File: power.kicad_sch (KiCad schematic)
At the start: 49 parts, among them J201 Barrel_Jack_MountingPin, J202 -, J203 -, Q201 AOD4185, U101 74HC04, U102 74HC08, U103 74HC32, U201 MP9942GJ

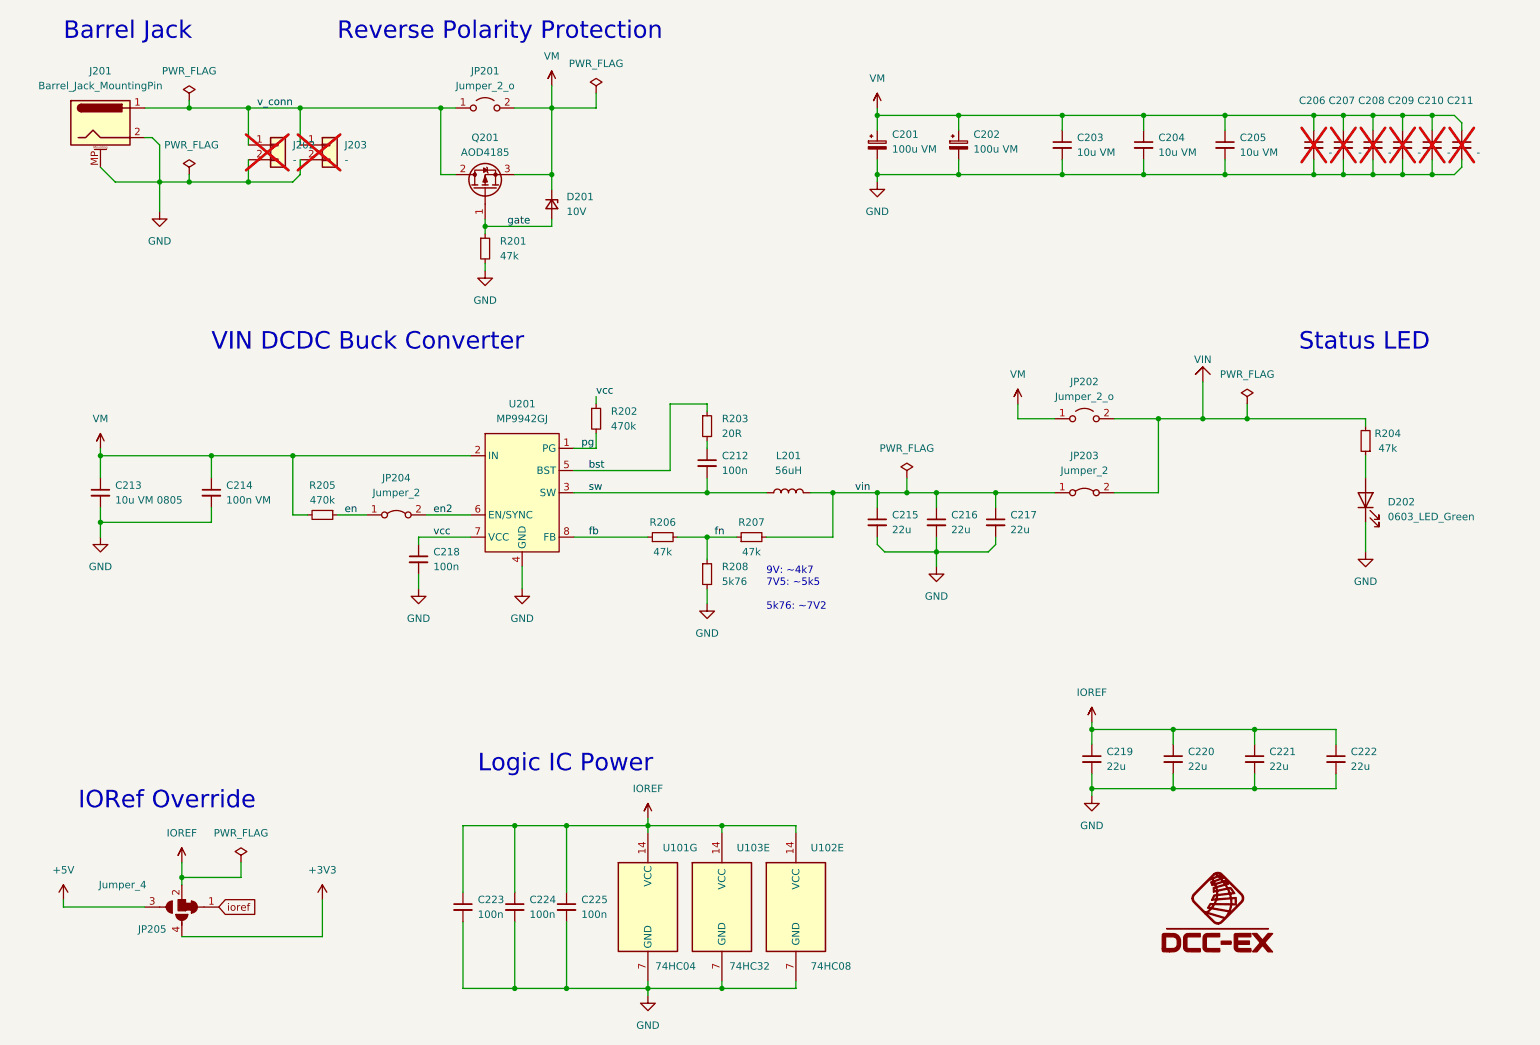
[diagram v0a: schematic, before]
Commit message: Convert to native KiCad & rework BOM to JLCPCB Basic Parts.
1) Use a KiCad template for an Arduino motor shield as the base.

2) DC-DC Buck converter shows no longer available, select new
   component from JLCPCB's basic list and re-work circuit as necessary.

3) Reworked BOM to use as many JLCPCB basic components as possible.

4) Reworked BOM so all components are in-stock at JLCPCB.

5) Switched to TSSOP for the 74HC logic to save space.e

6) Switched to all KiCad native symbols, which required:
   - Reworking some of the solder jumper logic.
   - Renaming VM to Vdrive.
   - Renaming IOREF to VBUS.
   - Renaming VIN to VCOM.
   - Creating a new symbol library for this project.
   - Creating a new footprint library for this project.
   - Moving a LOT of symbols from _my symbols to KiCad native symbols.

7) Removed unnecessary decoupling capacitors from 74HC logic, a single
   100nF is sufficient.

8) Removed unnecessary decoupling capacitors from Vdrive, not sure why
   they were there.

9) Did a new layout of the board:
   - Started with the DRV8874 chips, layout per data sheet, include
     large multi-layer ground plane to dissipate heat.
   - Moved on to DC-DC buck converter, layout per data sheet, include
     large ground plane to dissipate heat.
   - Put the configuration jumpers in ROUGHLY the same place.
   - Put the I2C OLED and STEMMA connectors in the same place, moved
     the 0.1" pin header connector slightly.

10) Routed everything.

11) Made sure it 100% passed ERC.

12) Made sure it 100% passed DRC.
    - A few exclusions for mechanical holes and silk off the board from the
      template.

13) Uploaded to JLCPCB to price.  Adjusted BOM again due to inventory shortages.
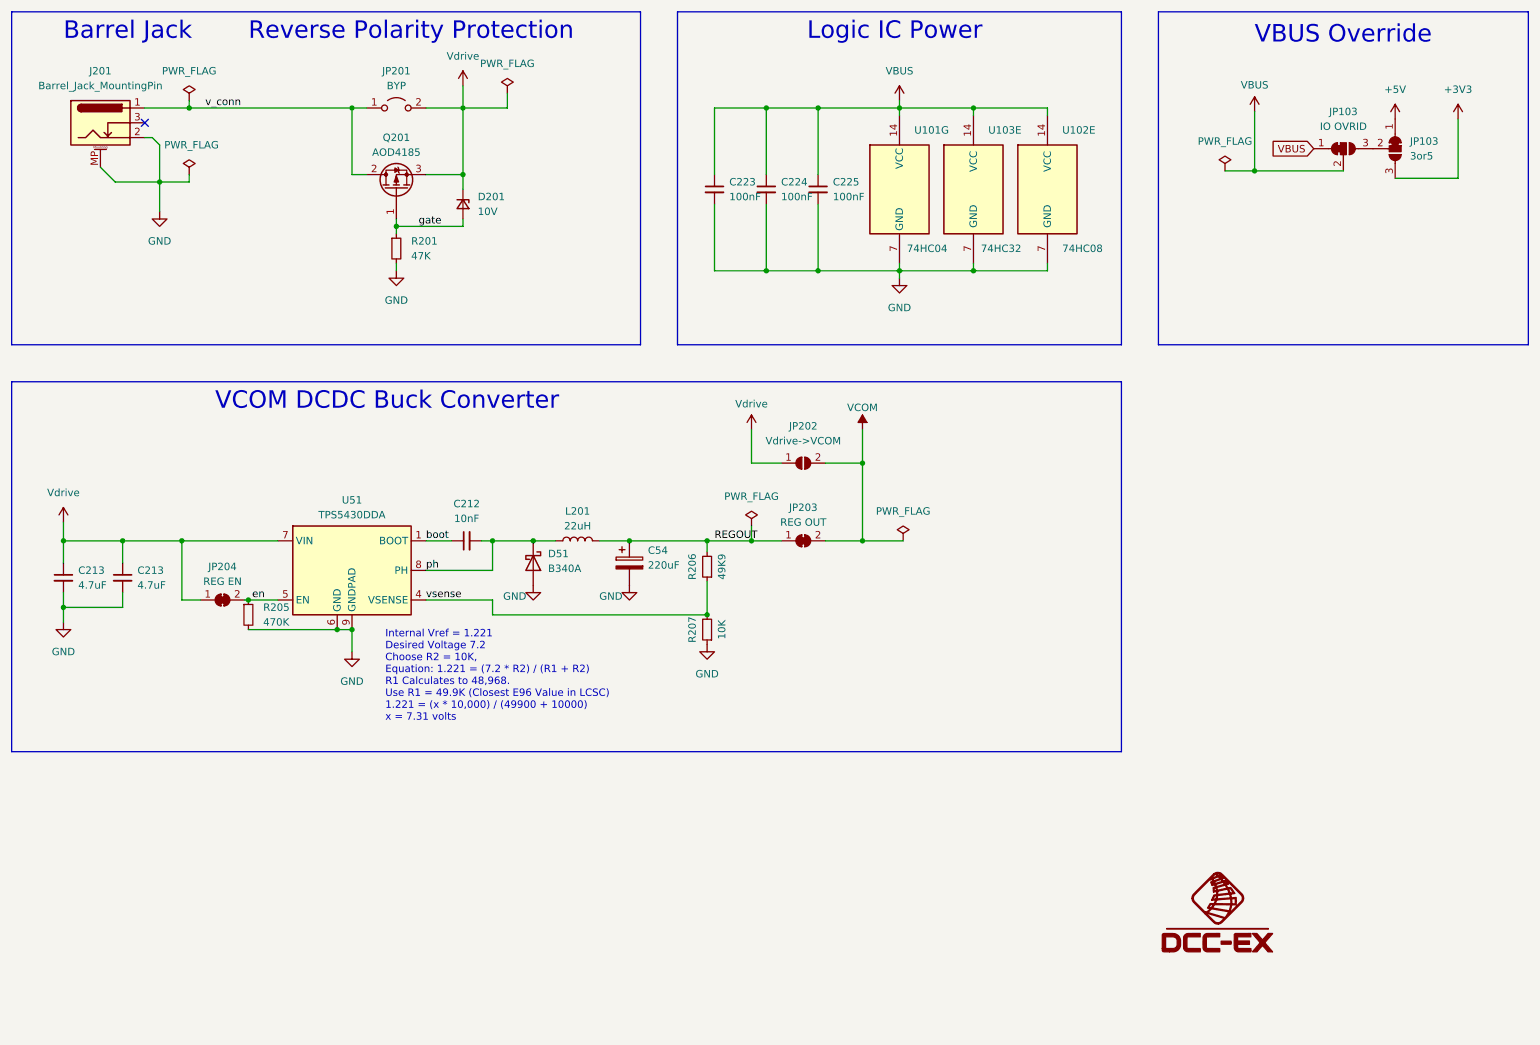
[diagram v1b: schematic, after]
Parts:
- removed C201, C202: 100u VM, Capacitor_SMD:CP_Elec_6.3x7.7, symbol Device:C_Polarized_Small
- removed C203, C204, C205: 10u VM, Capacitor_SMD:C_1206_3216Metric, symbol Device:C_Small
- removed C206, C207, C208, C209, C210, C211: -, Capacitor_SMD:C_1210_3225Metric_Pad1.33x2.70mm_HandSolder, symbol Device:C_Small
- removed C214: 100n VM, _my:C_1005_(0402), symbol Device:C_Small
- removed C215, C216, C217, C219, C220, C221, C222: 22u, Capacitor_SMD:C_0805_2012Metric, symbol Device:C_Small
- removed C218: 100n, _my:C_1005_(0402), symbol Device:C_Small
- removed D202: 0603_LED_Green, LED_SMD:LED_0603_1608Metric, symbol Device:LED
- removed J202: -, _my:PinHeader_01x02_P5mm_Vertical_min, symbol Connector_Generic:Conn_01x02
- removed J203: -, _my:PinHeader_1x04_P2.54mm_Vertical_min_1, symbol Connector_Generic:Conn_01x02
- removed JP205: Jumper_4, _my:SolderJumper-4, symbol _my:SolderJumper_4
- removed R202: 470k, _my:R_1005_(0402), symbol Device:R_Small
- removed R203: 20R, _my:R_1005_(0402), symbol Device:R_Small
- removed R204: 47k, _my:R_1005_(0402), symbol Device:R_Small
- removed R208: 5k76, _my:R_1005_(0402), symbol Device:R_Small
- removed U201: MP9942GJ, _my:TSOT23-8, symbol _my:MP9942GJ
- added C213: 4.7uF, Capacitor_SMD:C_1206_3216Metric, symbol Device:C_Small
- added C54: 220uF, Capacitor_Tantalum_SMD:CP_EIA-7343-31_Kemet-D, symbol Device:C_Polarized
- added D51: B340A, Diode_SMD:D_SMA, symbol Device:D_Schottky
- added JP103: IO OVRID, Jumper:SolderJumper-3_P1.3mm_Bridged12_RoundedPad1.0x1.5mm, symbol Jumper:SolderJumper_3_Bridged12
- added JP103: 3or5, Jumper:SolderJumper-3_P1.3mm_Bridged12_RoundedPad1.0x1.5mm, symbol Jumper:SolderJumper_3_Bridged12
- added U51: TPS5430DDA, Package_SO:TI_SO-PowerPAD-8_ThermalVias, symbol Regulator_Switching:TPS5430DDA
- C212: value 100n -> 10nF; footprint _my:C_1005_(0402) -> Capacitor_SMD:C_0402_1005Metric; LCSC Part # C1525 -> C15195
- C213: value 10u VM 0805 -> 4.7uF; footprint Capacitor_SMD:C_0805_2012Metric -> Capacitor_SMD:C_1206_3216Metric; LCSC Part # C440198 -> C29823
- C223, C224, C225: value 100n -> 100nF; footprint _my:C_1005_(0402) -> Capacitor_SMD:C_0402_1005Metric; LCSC Part # C1525 -> C307331
- J201: footprint _my:BarrelJack_2.1mm_SMD -> DCC-EX-Footprints:DC-S050-200; symbol Connector:Barrel_Jack_MountingPin -> Connector:Barrel_Jack_Switch_MountingPin; rohs_cert_or_in_datasheet n -> y
- JP201: value Jumper_2_o -> BYP
- JP202: value Jumper_2_o -> Vdrive->VCOM; symbol Jumper:Jumper_2_Open -> Jumper:SolderJumper_2_Open; now in the parts list
- JP203: value Jumper_2 -> REG OUT; footprint _my:SolderJumper-2_P1.3mm_Bridged -> Jumper:SolderJumper-2_P1.3mm_Bridged_RoundedPad1.0x1.5mm; symbol Jumper:Jumper_2_Bridged -> Jumper:SolderJumper_2_Bridged; now in the parts list
- JP204: value Jumper_2 -> REG EN; footprint _my:SolderJumper-2_P1.3mm_Bridged -> Jumper:SolderJumper-2_P1.3mm_Bridged_RoundedPad1.0x1.5mm; symbol Jumper:Jumper_2_Bridged -> Jumper:SolderJumper_2_Bridged; now in the parts list
- L201: value 56uH -> 22uH; footprint _my:L_PSPMAA0805 -> DCC-EX-Footprints:L_6.7x7.2_H5; LCSC Part # C2962890 -> C5189963
- Q201: symbol _my:AOD4185 -> Transistor_FET:IRF4905
- R201: value 47k -> 47K; footprint _my:R_1005_(0402) -> Resistor_SMD:R_0402_1005Metric; LCSC Part # C163440 -> C25792
- R205: value 470k -> 470K; footprint _my:R_1005_(0402) -> Resistor_SMD:R_0402_1005Metric; LCSC Part # C137865 -> C25790
- R206: value 47k -> 49K9; footprint _my:R_1005_(0402) -> Resistor_SMD:R_0402_1005Metric; LCSC Part # C163440 -> C25897
- R207: value 47k -> 10K; footprint _my:R_1005_(0402) -> Resistor_SMD:R_0402_1005Metric; LCSC Part # C163440 -> C25744
- U101: footprint Package_SO:SO-14_3.9x8.65mm_P1.27mm -> Package_SO:TSSOP-14_4.4x5mm_P0.65mm; LCSC Part # C5590 -> C80000
- U102: footprint Package_SO:SO-14_3.9x8.65mm_P1.27mm -> Package_SO:TSSOP-14_4.4x5mm_P0.65mm; LCSC Part # C5593 -> C80001
- U103: footprint Package_SO:SO-14_3.9x8.65mm_P1.27mm -> Package_SO:TSSOP-14_4.4x5mm_P0.65mm; LCSC Part # C5632 -> C282335
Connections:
- net en2 is gone; now on net en: JP204.2 (B)
- net +3V3: now also JP103.3 (B)
- net +5V: now also JP103.1 (A)
- net GND: now also R205.2, R207.1, C213.2, C54.2, D51.2 (A), U51.6 (GND), U51.9 (GNDPAD)
- net en: now also U51.5 (EN); no longer JP204.1 (A)
- net boot: now reaches C212.1
- net boot: now also U51.1 (BOOT)
- net IOREF renamed VBUS
- net VBUS: now also JP103.1 (A), JP103.2 (C)
- net VIN renamed VCOM
- net VM renamed Vdrive
- net Vdrive: now also JP204.1 (A), C213.1, U51.7 (VIN); no longer R205.2
- net fb renamed vsense
- net vsense: now also R207.2, U51.4 (VSENSE)
- net fn renamed REGOUT
- net REGOUT: now also JP203.1 (A), L201.2, C54.1; no longer R207.1
- net sw renamed ph
- net ph: now also D51.1 (K), U51.8 (PH)
- removed net vin: JP203.1 (A), L201.2, R207.2
- new net: JP103.2 (C), JP103.3 (B)
- no-connect marks 0 -> 1
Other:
- note added: "Internal Vref = 1.221 Desired Voltage 7.2 Choose R2 = 10K, Equation: 1.221 = (7.2 * R2) / (R1 + R2) R1 Calculates to 48,968. Use R1 = 49.9K (Closest E96 Value in LCSC) 1.221 = (x * 10,000) / (49900 + 10000) x = 7.31 volts"
- note added: "VBUS Override"
- note added: "VCOM DCDC Buck Converter"
- note removed: "9V: ~4k7 7V5: ~5k5 5k76: ~7V2"
- note removed: "IORef Override"
- note removed: "Status LED"
- note removed: "VIN DCDC Buck Converter"
- moved on the sheet: C212, C213, C223, C224, C225, D201, JP201, L201, Q201, R201, R205, R206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

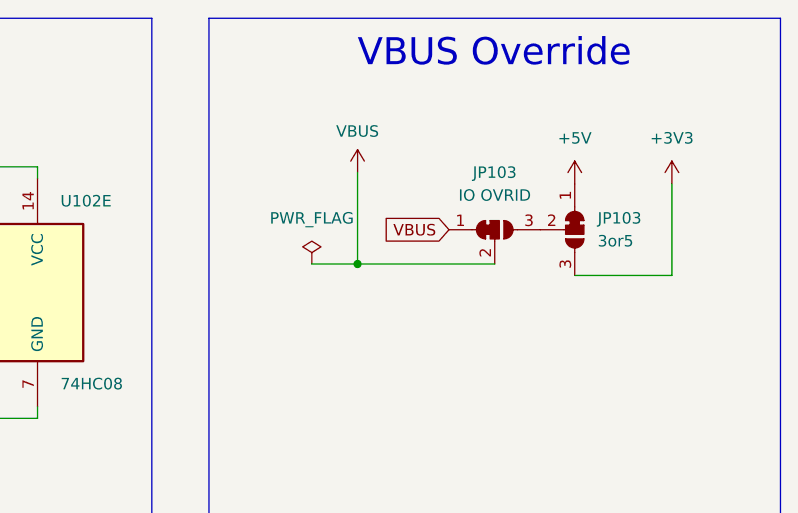
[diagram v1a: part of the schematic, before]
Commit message: IOREF detection to MOSFET, new indicator LEDs, reduce capacitor size.
1) Replaced the OpAmp & passives that determined IOREF 3 or 5 with a
   P-Channel MOSFET that does the same thing for less cost, components,
   and board space.

2) Changed indicator LEDs to be RED/GREEN single units.  When on DCC
   they will light RED+GREEN = YELLOW.  When driving a DC load (e.g.
   a motor, or even DC track with PWM) they will light either RED or
   GREEN to indicate direction.  They will also show address 0 stretching
   by changing hue.

3) Reduced the size of several capacitors, updated to more capable parts,
   selecting units that had high stock at LCSC & low cost.

4) Reworked traces to accomodate all of the above and generate some minor
   improvements in trace routing.
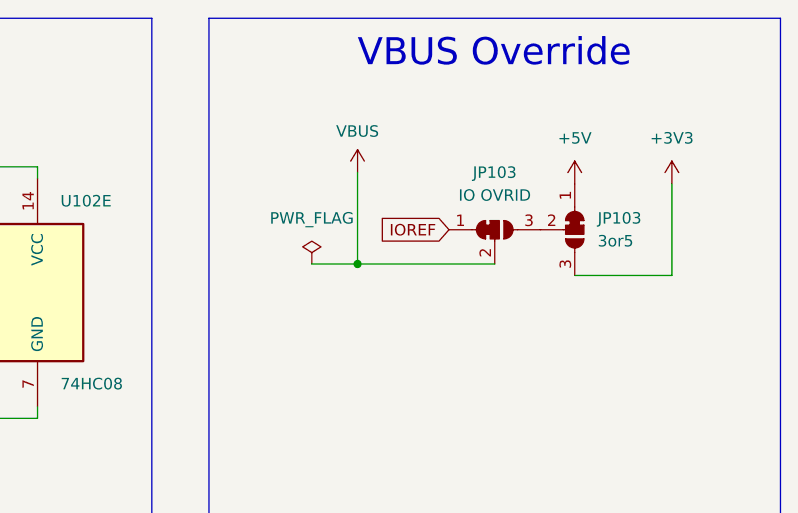
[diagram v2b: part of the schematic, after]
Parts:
- C213: footprint Capacitor_SMD:C_1206_3216Metric -> Capacitor_SMD:C_0805_2012Metric; LCSC Part # C29823 -> C98192
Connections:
- net VBUS: no longer JP103.1 (A)
- new net IOREF: JP103.1 (A)
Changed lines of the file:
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@@
     (effects (font (size 1.27 1.27)) (justify left bottom))
   )
-  (global_label "VBUS" (shape input) (at 242.57 42.545 180) (fields_autoplaced)
+  (global_label "IOREF" (shape input) (at 242.57 42.545 180) (fields_autoplaced)
     (effects (font (size 1.27 1.27)) (justify right))
-    (property "Intersheetrefs" "${INTERSHEET_REFS}" (at 235.1354 42.545 0)
+    (property "Intersheetrefs" "${INTERSHEET_REFS}" (at 234.0468 42.545 0)
       (effects (font (size 1.27 1.27)) (justify right) hide)
     )
@@
       (effects (font (size 1.27 1.27)) (justify left))
     )
-    (property "Footprint" "Capacitor_SMD:C_1206_3216Metric" (at 38.1 116.205 0)
+    (property "Footprint" "Capacitor_SMD:C_0805_2012Metric" (at 38.1 116.205 0)
       (effects (font (size 1.27 1.27)) hide)
     )
@@
       (effects (font (size 1.27 1.27)) hide)
     )
-    (property "LCSC Part #" "C29823" (at 38.1 116.205 0)
+    (property "LCSC Part #" "C98192" (at 38.1 116.205 0)
       (effects (font (size 1.27 1.27)) hide)
     )
@@
       (effects (font (size 1.27 1.27)) hide)
     )
-    (property "Description" "50V 4.7uF X7R ±10% 1206 Multilayer Ceramic Capacitors MLCC - SMD/SMT ROHS" (at 38.1 116.205 0)
+    (property "Description" "50V 4.7uF X5R ±10% 0805 Multilayer Ceramic Capacitors MLCC - SMD/SMT ROHS" (at 38.1 116.205 0)
       (effects (font (size 1.27 1.27)) hide)
     )
@@
       (effects (font (size 1.27 1.27)) (justify left))
     )
-    (property "Footprint" "Capacitor_SMD:C_1206_3216Metric" (at 27.94 116.205 0)
+    (property "Footprint" "Capacitor_SMD:C_0805_2012Metric" (at 27.94 116.205 0)
       (effects (font (size 1.27 1.27)) hide)
     )
@@
       (effects (font (size 1.27 1.27)) hide)
     )
-    (property "LCSC Part #" "C29823" (at 27.94 116.205 0)
+    (property "LCSC Part #" "C98192" (at 27.94 116.205 0)
       (effects (font (size 1.27 1.27)) hide)
     )
@@
       (effects (font (size 1.27 1.27)) hide)
     )
-    (property "Description" "50V 4.7uF X7R ±10% 1206 Multilayer Ceramic Capacitors MLCC - SMD/SMT ROHS" (at 27.94 116.205 0)
-      (effects (font (size 1.27 1.27)) hide)
-    )
+    (property "Description" "50V 4.7uF X5R ±10% 0805 Multilayer Ceramic Capacitors MLCC - SMD/SMT ROHS" (at 27.94 116.205 0)
+      (effects (font (size 1.27 1.27)) hide)
+    )
